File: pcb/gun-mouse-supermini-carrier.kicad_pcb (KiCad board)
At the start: 2 copper layers, 52 x 82 mm, 29 parts, among them SW1 RKJXV1224005, SW2 D2FC-F-7N(20M)

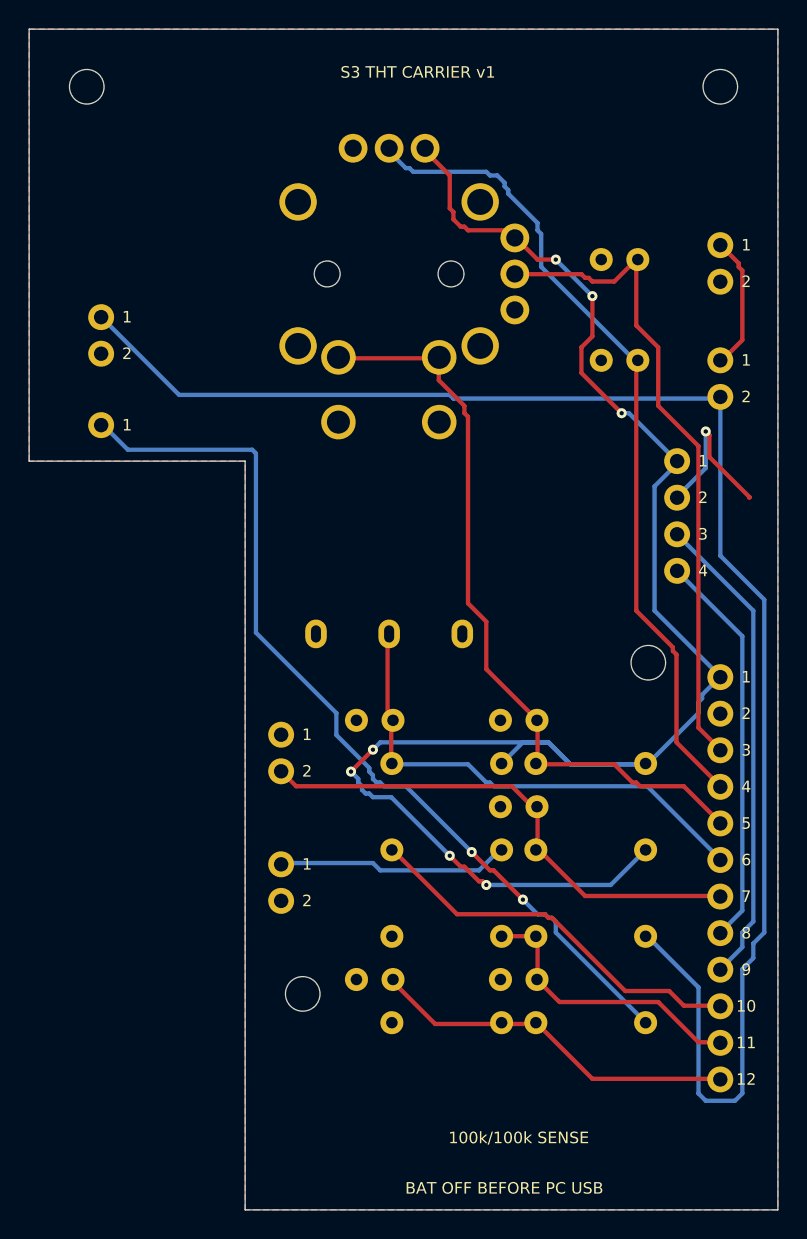
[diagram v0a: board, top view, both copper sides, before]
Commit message: 第二代：修正摇杆孔位，增加板载电源和开放底座，交付OBJ模型
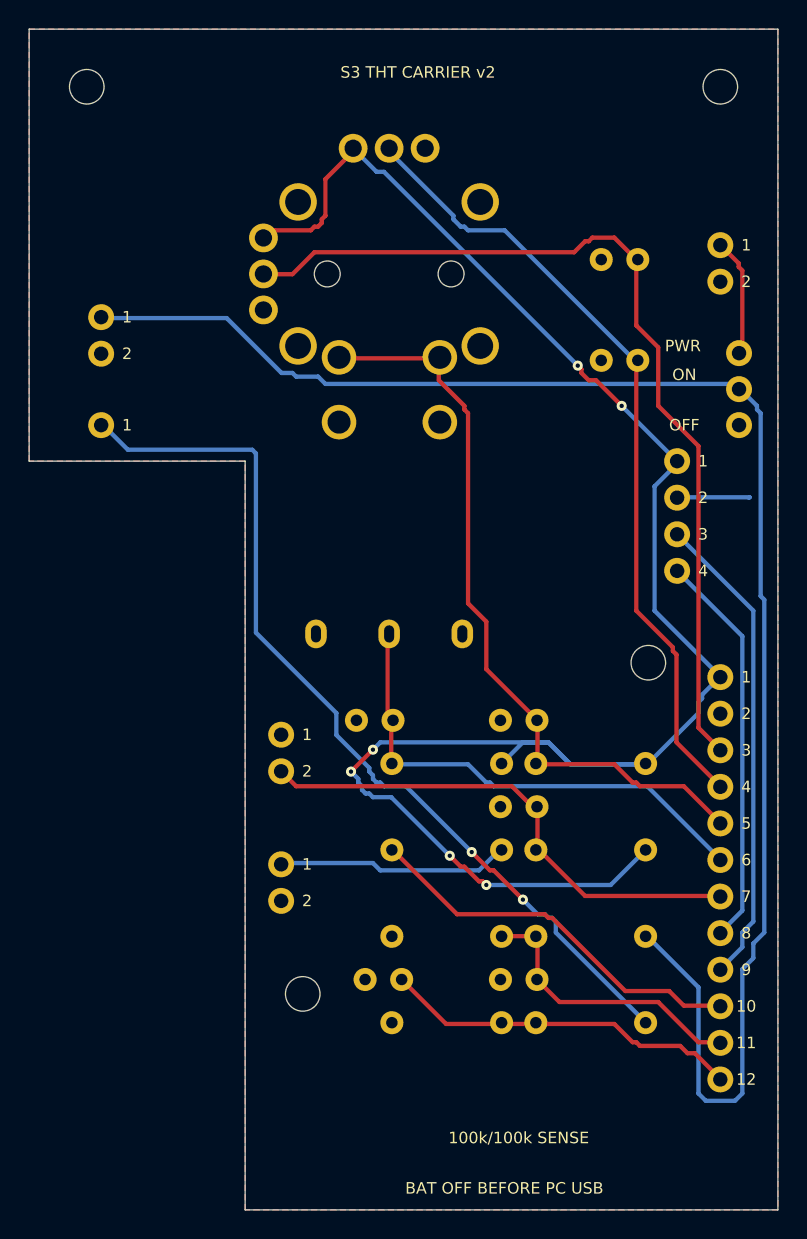
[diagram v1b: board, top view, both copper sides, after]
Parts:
- J_SWITCH: value Labelled solder wires -> SS-12D01-G030
- moved J_SWITCH 2.39 mm to (54.3, 30.0)
- moved SW1 1.43 mm to (30.0, 22.0)
- moved C_RAIL 0.60 mm to (29.6, 71.0)
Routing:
- net JOY_X: track 46.0 -> 64.3 mm
- net 3V3: track 117.7 -> 127.4 mm, vias 7 -> 6
- net GND: track 11.3 -> 5.18 mm, vias 1 -> 0
- net JOY_Y: track 57.7 -> 55.9 mm
- net BAT_SW: track 111.7 -> 112.9 mm
- net BAT_RAW: track 9.52 -> 8.48 mm
- net VBUS_DET: track 26.4 -> 25.5 mm
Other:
- board text added: "OFF"
- board text added: "ON"
- board text added: "PWR"
- board text added: "S3 THT CARRIER v2"
- board text removed: "S3 THT CARRIER v1"

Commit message: 更新模块直插结构与完整装配预览模型
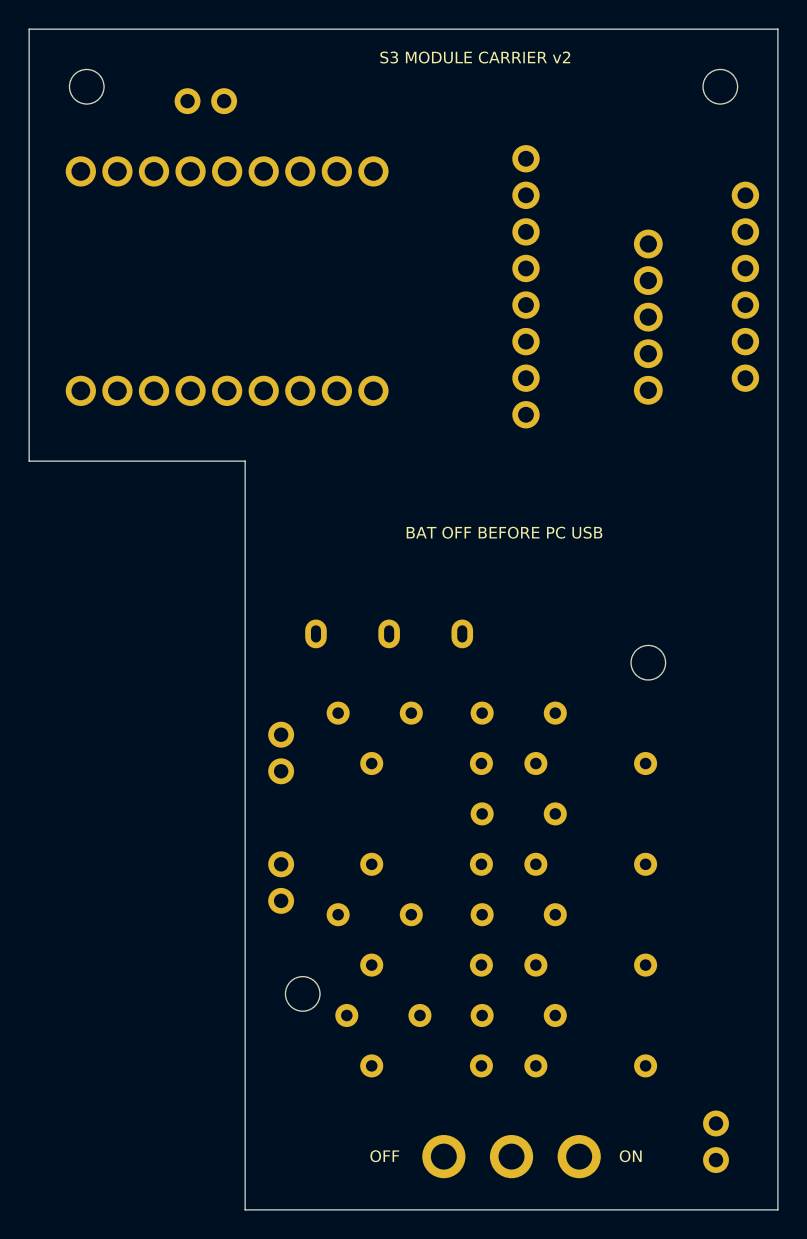
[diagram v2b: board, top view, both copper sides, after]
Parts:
- removed J_MODULE_RAIL: Labelled solder wires, GunMouseHandSolder:J_MODULE_RAIL
- J_GY: value Labelled solder wires -> GY-601N1-LSM6DSV16X 8+6
- J_MCU: value Labelled solder wires -> ESP32-S3 SuperMini 2x9
- J_SWITCH: value SS-12D01-G030 -> SS12D10 G5
- SW1: value RKJXV1224005 -> HW-504 34x26mm; moved to B.Cu
- moved J_BAT 61.0 mm to (52.7, 81.0)
- moved J_SWITCH 55.6 mm to (38.5, 83.3)
- moved C_JOY_X 46.0 mm to (39.0, 66.5)
- moved J_MCU 43.9 mm to (18.8, 22.5)
- moved C_JOY_Y 42.1 mm to (29.0, 66.5)
- moved SW1 18.2 mm to (48.0, 25.0), turned to 180 degrees
- moved J_MODULE_BAT 16.2 mm to (16.0, 10.0)
- moved J_GY 12.3 mm to (47.1, 23.0)
- moved R_RAIL_L 3.31 mm to (32.6, 77.0)
- moved R_RAIL_H 3.00 mm to (44.0, 77.0)
- moved C_BAT 2.50 mm to (39.0, 73.5)
- moved C_RAIL 2.50 mm to (29.6, 73.5)
- moved R_BAT_L 2.44 mm to (32.6, 70.0)
- moved R_BAT_H 2.00 mm to (44.0, 70.0)
- moved R_TOUCH 1.72 mm to (32.6, 63.0)
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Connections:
- J_MCU pad 1: 3V3 -> (no net)
- J_MCU pad 10: TOUCH -> VBUS_SHARED
- J_MCU pad 11: VBAT_ADC -> GND
- J_MCU pad 12: VBUS_DET -> 3V3
- J_MCU pad 2: GND -> (no net)
- J_MCU pad 5: JOY_SW -> (no net)
- J_MCU pad 6: BTN_R -> JOY_SW
- J_MCU pad 7: TRIG -> SDA
- J_MCU pad 8: SDA -> SCL
- J_MCU pad 9: SCL -> TOUCH
- SW1 pad 2: JOY_X -> 3V3
- SW1 pad 3: 3V3 -> JOY_X
- SW1 pad 4: 3V3 -> JOY_Y
- SW1 pad 5: JOY_Y -> JOY_SW
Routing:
- net 3V3: track 127.4 -> 0.00 mm, vias 6 -> 0
- net BAT_SW: track 112.9 -> 0.00 mm
- net JOY_X: track 64.3 -> 0.00 mm
- net VBUS_SHARED: track 64.3 -> 0.00 mm, vias 2 -> 0
- net JOY_Y: track 55.9 -> 0.00 mm
- net JOY_SW: track 52.9 -> 0.00 mm
- net TRIG: track 36.3 -> 0.00 mm
- net BTN_R: track 35.4 -> 0.00 mm
- net SCL: track 33.5 -> 0.00 mm
- net SDA: track 27.8 -> 0.00 mm
- net TOUCH: track 27.5 -> 0.00 mm
- net VBUS_DET: track 25.5 -> 0.00 mm
- net VBAT_ADC: track 20.5 -> 0.00 mm
- net TOUCH_ELECTRODE: track 16.3 -> 0.00 mm
- net BAT_RAW: track 8.48 -> 0.00 mm
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- removed copper zone on B.Cu, net GND
- removed copper zone on F.Cu, net GND
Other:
- board text added: "C_BAT.1 VBAT_ADC"
- board text added: "C_BAT.2 GND"
- board text added: "C_JOY_SW.1 JOY_SW"
- board text added: "C_JOY_SW.2 GND"
- board text added: "C_JOY_X.1 JOY_X"
- board text added: "C_JOY_X.2 GND"
- board text added: "C_JOY_Y.1 JOY_Y"
- board text added: "C_JOY_Y.2 GND"
- board text added: "C_RAIL.1 VBUS_DET"
- board text added: "C_RAIL.2 GND"
- board text added: "C_RIGHT.1 BTN_R"
- board text added: "C_RIGHT.2 GND"
- board text added: "C_TRIG.1 TRIG"
- board text added: "C_TRIG.2 GND"
- board text added: "J_BAT.1 BAT_RAW"
- board text added: "J_BAT.2 GND"
- board text added: "J_GY.1 VCC"
- board text added: "J_GY.10 INTOUT"
- board text added: "J_GY.11 DT"
- board text added: "J_GY.12 RC"
- board text added: "J_GY.13 GND"
- board text added: "J_GY.14 VCC"
- board text added: "J_GY.2 GND"
- board text added: "J_GY.3 SCL"
- board text added: "J_GY.4 SDA"
- board text added: "J_GY.5 SA0"
- board text added: "J_GY.6 CS"
- board text added: "J_GY.7 INT1"
- board text added: "J_GY.8 INT2"
- board text added: "J_GY.9 PS"
- board text added: "J_MCU.1 TX43"
- board text added: "J_MCU.10 5V"
- board text added: "J_MCU.11 GND"
- board text added: "J_MCU.12 3V3"
- board text added: "J_MCU.13 13"
- board text added: "J_MCU.14 12"
- board text added: "J_MCU.15 11"
- board text added: "J_MCU.16 10"
- board text added: "J_MCU.17 9"
- board text added: "J_MCU.18 8"
- board text added: "J_MCU.2 RX44"
- board text added: "J_MCU.3 1"
- board text added: "J_MCU.4 2"
- board text added: "J_MCU.5 3"
- board text added: "J_MCU.6 4"
- board text added: "J_MCU.7 5"
- board text added: "J_MCU.8 6"
- board text added: "J_MCU.9 7"
- board text added: "J_MODULE_BAT.1 BAT_SW"
- board text added: "J_MODULE_BAT.2 GND"
- board text added: "J_SWITCH.1 BAT_RAW"
- board text added: "J_SWITCH.2 BAT_SW"
- board text added: "J_SWITCH.3 NC"
- board text added: "J_TOUCH.1 TOUCH_ELECTRODE"
- board text added: "J_TOUCH.2 GND"
- board text added: "J_TRIG.1 GND"
- board text added: "J_TRIG.2 TRIG"
- board text added: "R_BAT_H.1 BAT_SW"
- board text added: "R_BAT_H.2 VBAT_ADC"
- board text added: "R_BAT_L.1 VBAT_ADC"
- board text added: "R_BAT_L.2 GND"
- board text added: "R_JOY.1 3V3"
- board text added: "R_JOY.2 JOY_SW"
- board text added: "R_RAIL_H.1 VBUS_SHARED"
- board text added: "R_RAIL_H.2 VBUS_DET"
- board text added: "R_RAIL_L.1 VBUS_DET"
- board text added: "R_RAIL_L.2 GND"
- board text added: "R_RIGHT.1 3V3"
- board text added: "R_RIGHT.2 BTN_R"
- board text added: "R_TOUCH.1 TOUCH_ELECTRODE"
- board text added: "R_TOUCH.2 TOUCH"
- board text added: "R_TRIG.1 3V3"
- board text added: "R_TRIG.2 TRIG"
- board text added: "S3 MODULE CARRIER v2"
- board text added: "SW1.1 GND"
- board text added: "SW1.2 3V3"
- board text added: "SW1.3 JOY_X"
- board text added: "SW1.4 JOY_Y"
- board text added: "SW1.5 JOY_SW"
- board text added: "SW2.1 GND"
- board text added: "SW2.2 BTN_R"
- board text added: "SW2.3 NC"
- board text removed: "1"
- board text removed: "10"
- board text removed: "100k/100k SENSE"
- board text removed: "11"
- board text removed: "12"
- board text removed: "2"
- board text removed: "3"
- board text removed: "3V3"
- board text removed: "4"
- board text removed: "5"
- board text removed: "6"
- board text removed: "7"
- board text removed: "8"
- board text removed: "9"
- board text removed: "BAT_RAW"
- board text removed: "BAT_SW"
- board text removed: "BTN_R"
- board text removed: "C_BAT"
- board text removed: "C_JOY_SW"
- board text removed: "C_JOY_X"
- board text removed: "C_JOY_Y"
- board text removed: "C_RAIL"
- board text removed: "C_RIGHT"
- board text removed: "C_TRIG"
- board text removed: "GND"
- board text removed: "JOY_SW"
- board text removed: "JOY_X"
- board text removed: "JOY_Y"
- board text removed: "PWR"
- board text removed: "R_BAT_H"
- board text removed: "R_BAT_L"
- board text removed: "R_JOY"
- board text removed: "R_RAIL_H"
- board text removed: "R_RAIL_L"
- board text removed: "R_RIGHT"
- board text removed: "R_TOUCH"
- board text removed: "R_TRIG"
- board text removed: "S3 THT CARRIER v2"
- board text removed: "SCL"
- board text removed: "SDA"
- board text removed: "TOUCH"
- board text removed: "TOUCH_ELECTRODE"
- board text removed: "TRIG"
- board text removed: "VBAT_ADC"
- board text removed: "VBUS_DET"
- board text removed: "VBUS_SHARED"

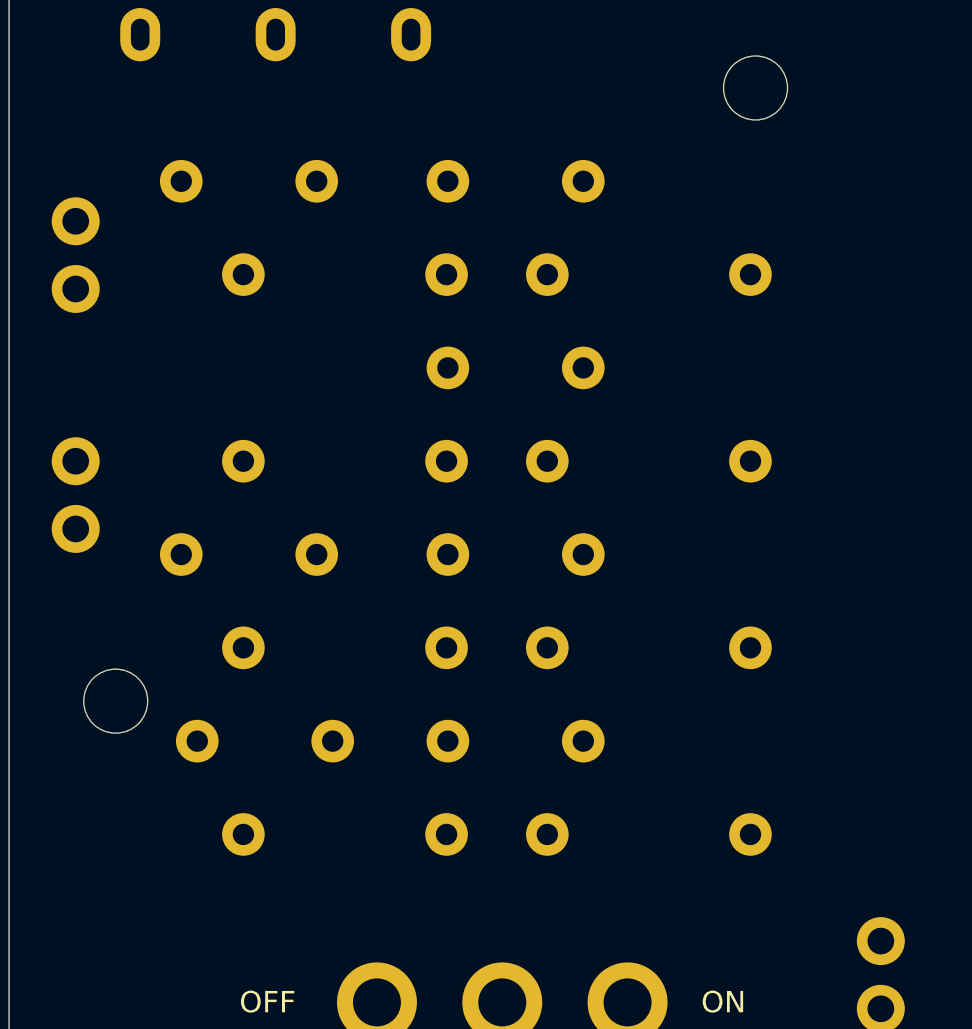
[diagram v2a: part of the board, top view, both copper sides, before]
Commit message: 精简供电监测与按键元件并扩大手焊焊盘
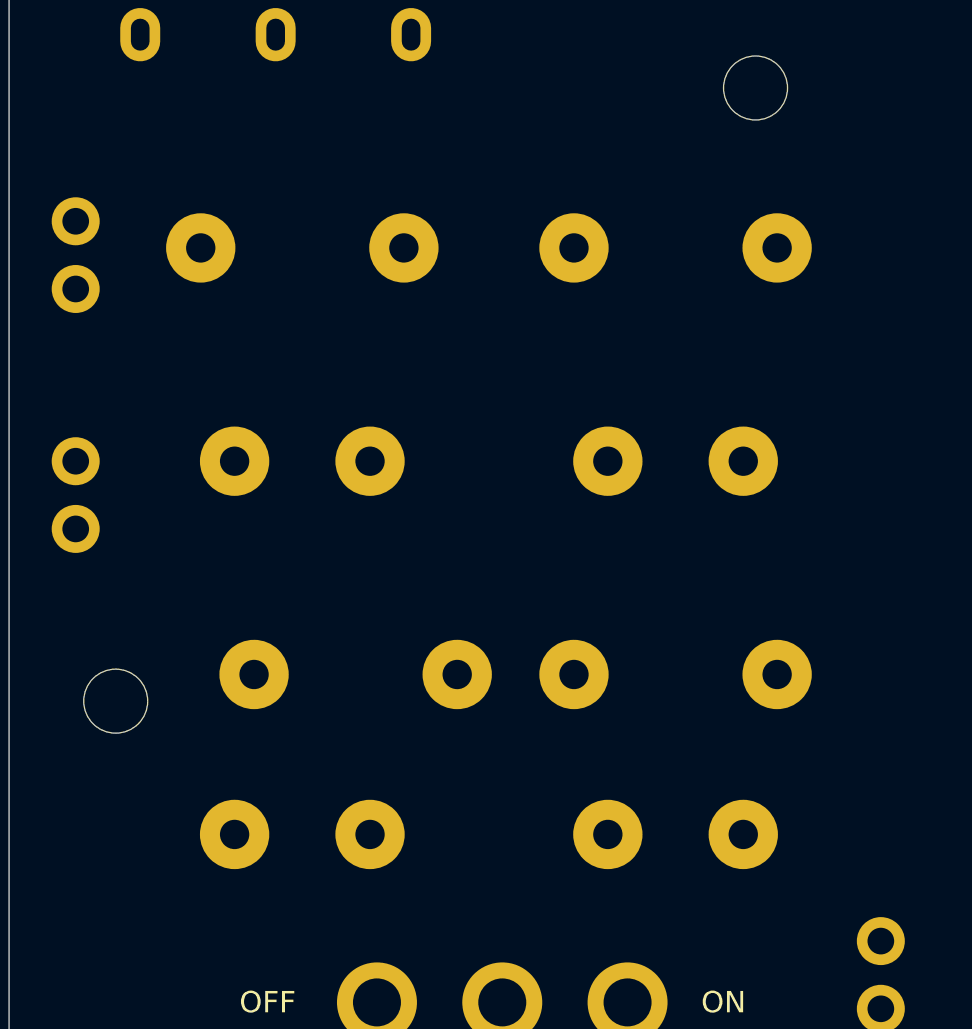
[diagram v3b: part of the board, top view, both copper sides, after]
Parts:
- removed C_JOY_SW: 100n, GunMouseHandSolder:C_JOY_SW
- removed C_RAIL: 100n, GunMouseHandSolder:C_RAIL
- removed C_RIGHT: 100n, GunMouseHandSolder:C_RIGHT
- removed R_JOY: 3.3k, GunMouseHandSolder:R_JOY
- removed R_RAIL_H: 100k, GunMouseHandSolder:R_RAIL_H
- removed R_RAIL_L: 100k, GunMouseHandSolder:R_RAIL_L
- removed R_RIGHT: 3.3k, GunMouseHandSolder:R_RIGHT
- moved C_JOY_Y 10.7 mm to (31.0, 77.0)
- moved C_JOY_X 8.73 mm to (31.0, 63.0)
- moved R_TOUCH 8.16 mm to (31.0, 55.0)
- moved R_TRIG 8.06 mm to (45.0, 55.0)
- moved C_BAT 6.95 mm to (45.0, 77.0)
- moved C_TRIG 6.95 mm to (45.0, 63.0)
- moved R_BAT_H 1.41 mm to (45.0, 71.0)
- moved R_BAT_L 1.08 mm to (33.0, 71.0)
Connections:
- J_MCU pad 10: VBUS_SHARED -> (no net)
- J_MCU pad 16: VBUS_DET -> (no net)
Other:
- board text removed: "C_JOY_SW.1 JOY_SW"
- board text removed: "C_JOY_SW.2 GND"
- board text removed: "C_RAIL.1 VBUS_DET"
- board text removed: "C_RAIL.2 GND"
- board text removed: "C_RIGHT.1 BTN_R"
- board text removed: "C_RIGHT.2 GND"
- board text removed: "R_JOY.1 3V3"
- board text removed: "R_JOY.2 JOY_SW"
- board text removed: "R_RAIL_H.1 VBUS_SHARED"
- board text removed: "R_RAIL_H.2 VBUS_DET"
- board text removed: "R_RAIL_L.1 VBUS_DET"
- board text removed: "R_RAIL_L.2 GND"
- board text removed: "R_RIGHT.1 3V3"
- board text removed: "R_RIGHT.2 BTN_R"

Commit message: 完成第二代真实铜层与手焊导线装配模型
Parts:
- C_BAT, C_JOY_X, C_JOY_Y, C_TRIG, J_BAT, J_GY, J_MCU, J_MODULE_BAT, J_SWITCH, J_TOUCH, J_TRIG, R_BAT_H, R_BAT_L, R_TOUCH, R_TRIG, SW2: moved to B.Cu
- SW1: moved to F.Cu
- turned C_BAT to 180 degrees
- turned C_JOY_X to 180 degrees
- turned C_JOY_Y to 180 degrees
- turned C_TRIG to 180 degrees
- turned J_BAT to 180 degrees
- turned J_GY to 180 degrees
- turned J_MCU to 180 degrees
- turned J_MODULE_BAT to 180 degrees
- turned J_SWITCH to 180 degrees
- turned J_TOUCH to 180 degrees
- turned J_TRIG to 180 degrees
- turned R_BAT_H to 180 degrees
- turned R_BAT_L to 180 degrees
- turned R_TOUCH to 180 degrees
- turned R_TRIG to 180 degrees
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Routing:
- net 3V3: track 0.00 -> 144.6 mm, vias 0 -> 2
- net BAT_SW: track 0.00 -> 105.7 mm
- net JOY_Y: track 0.00 -> 101.7 mm, vias 0 -> 1
- net JOY_X: track 0.00 -> 86.4 mm
- net VBAT_ADC: track 0.00 -> 60.9 mm
- net TRIG: track 0.00 -> 55.0 mm, vias 0 -> 1
- net TOUCH: track 0.00 -> 48.4 mm
- net JOY_SW: track 0.00 -> 45.4 mm
- net SCL: track 0.00 -> 23.0 mm
- net SDA: track 0.00 -> 22.3 mm
- net BTN_R: track 0.00 -> 21.6 mm, vias 0 -> 1
- net TOUCH_ELECTRODE: track 0.00 -> 15.6 mm
- net BAT_RAW: track 0.00 -> 10.8 mm
- added copper zone on B.Cu, net GND
- added copper zone on F.Cu, net GND

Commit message: 换侧保护支架并采用每行一颗的宽间距手焊布局
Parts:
- moved R_TOUCH 11.2 mm to (42.1, 56.5)
- moved C_JOY_X 11.1 mm to (42.1, 63.5)
- moved C_JOY_Y 11.1 mm to (42.1, 77.5)
- moved R_BAT_L 9.09 mm to (42.1, 70.5)
- moved R_BAT_H 8.94 mm to (37.0, 67.0)
- moved C_BAT 8.54 mm to (37.0, 74.0)
- moved C_TRIG 8.54 mm to (37.0, 60.0)
- moved R_TRIG 8.25 mm to (37.0, 53.0)
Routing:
- net GND: track 0.00 -> 19.4 mm, vias 0 -> 1
- net TOUCH_ELECTRODE: track 15.6 -> 28.6 mm
- net JOY_Y: track 101.7 -> 109.6 mm
- net SCL: track 23.0 -> 30.5 mm
- net 3V3: track 144.6 -> 151.1 mm, vias 2 -> 6
- net TRIG: track 55.0 -> 48.7 mm
- net JOY_X: track 86.4 -> 92.6 mm
- net BAT_SW: track 105.7 -> 103.1 mm, vias 0 -> 1
- net TOUCH: track 48.4 -> 47.0 mm
- net VBAT_ADC: track 60.9 -> 62.1 mm
